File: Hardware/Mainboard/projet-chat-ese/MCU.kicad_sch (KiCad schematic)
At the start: 23 parts, among them J401 Conn_ST_STDC14, J402 USB_C_Receptacle_USB2.0_16P, J403 UART, SW401 SW_SPST, U401 STM32G431CBUx, U402 USBLC6-2SC6, Y401 MCSJK-7U-16.00-10-30-80-B-30

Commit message: On a pas de wiork trtee anyway
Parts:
- J403: footprint Connector_JST:JST_EH_B4B-EH-A_1x04_P2.50mm_Vertical -> Connector_JST:JST_PH_B4B-PH-K_1x04_P2.00mm_Vertical
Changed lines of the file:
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@@
 			)
 		)
-		(property "Footprint" "Connector_JST:JST_EH_B4B-EH-A_1x04_P2.50mm_Vertical"
+		(property "Footprint" "Connector_JST:JST_PH_B4B-PH-K_1x04_P2.00mm_Vertical"
 			(at 213.36 99.06 0)
 			(effects

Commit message: Finishing PCB
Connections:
- net +3.3V: no longer J403.1 (Pin_1)
- net +5V: now also J403.1 (Pin_1)
- net BT_~{RST}: now also U401.39 (PC10); no longer U401.25 (PB12)
- net GND: now also J403.3 (Pin_3)
- net MOT1_Imes: now also U401.11 (PA3); no longer U401.28 (PB15)
- net UART1_Rx: now also J403.2 (Pin_2), U401.38 (PA15); no longer J403.3 (Pin_3), U401.11 (PA3)
- net UART1_Tx: no longer names the net of U401.10 (PA2)
- net UART1_Tx: no longer J403.2 (Pin_2)
- no-connect marks 15 -> 16
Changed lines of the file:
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@@
 	)
 	(junction
+		(at 207.01 104.14)
+		(diameter 0)
+		(color 0 0 0 0)
+	)
+	(junction
 		(at 252.73 151.13)
 		(diameter 0)
@@
 	)
 	(no_connect
-		(at 107.95 82.55)
-	)
-	(no_connect
 		(at 266.7 137.16)
 	)
@@
 	)
 	(no_connect
-		(at 72.39 67.31)
+		(at 72.39 113.03)
 	)
 	(no_connect
@@
 	)
 	(no_connect
+		(at 107.95 49.53)
+	)
+	(no_connect
+		(at 72.39 120.65)
+	)
+	(no_connect
 		(at 72.39 92.71)
 	)
@@
 	(wire
 		(pts
+			(xy 69.85 67.31) (xy 72.39 67.31)
+		)
+		(stroke
+			(width 0)
+			(type default)
+		)
+	)
+	(wire
+		(pts
 			(xy 41.91 52.07) (xy 38.1 52.07)
 		)
@@
 	(wire
 		(pts
-			(xy 69.85 120.65) (xy 72.39 120.65)
+			(xy 207.01 41.91) (xy 214.63 41.91)
 		)
 		(stroke
@@
 	(wire
 		(pts
-			(xy 207.01 41.91) (xy 214.63 41.91)
+			(xy 196.85 99.06) (xy 208.28 99.06)
 		)
 		(stroke
@@
 	(wire
 		(pts
-			(xy 252.73 151.13) (xy 251.46 151.13)
+			(xy 207.01 101.6) (xy 207.01 104.14)
 		)
 		(stroke
@@
 	(wire
 		(pts
-			(xy 72.39 54.61) (xy 66.04 54.61)
+			(xy 252.73 151.13) (xy 251.46 151.13)
 		)
 		(stroke
@@
 	(wire
 		(pts
-			(xy 107.95 57.15) (xy 111.76 57.15)
+			(xy 72.39 54.61) (xy 66.04 54.61)
 		)
 		(stroke
@@
 	(wire
 		(pts
-			(xy 41.91 102.87) (xy 46.99 102.87)
+			(xy 107.95 57.15) (xy 111.76 57.15)
 		)
 		(stroke
@@
 	(wire
 		(pts
-			(xy 208.28 96.52) (xy 207.01 96.52)
+			(xy 41.91 102.87) (xy 46.99 102.87)
 		)
 		(stroke
@@
 	(wire
 		(pts
-			(xy 69.85 107.95) (xy 72.39 107.95)
+			(xy 208.28 96.52) (xy 207.01 96.52)
 		)
 		(stroke
@@
 	(wire
 		(pts
-			(xy 119.38 52.07) (xy 107.95 52.07)
+			(xy 69.85 107.95) (xy 72.39 107.95)
 		)
 		(stroke
@@
 		)
 	)
+	(wire
+		(pts
+			(xy 208.28 101.6) (xy 207.01 101.6)
+		)
+		(stroke
+			(width 0)
+			(type default)
+		)
+	)
 	(polyline
 		(pts
@@
 	(wire
 		(pts
-			(xy 119.38 49.53) (xy 107.95 49.53)
-		)
-		(stroke
-			(width 0)
-			(type default)
-		)
-	)
-	(wire
-		(pts
 			(xy 240.03 38.1) (xy 240.03 40.64)
 		)
@@
 	(wire
 		(pts
-			(xy 69.85 87.63) (xy 72.39 87.63)
+			(xy 111.76 52.07) (xy 107.95 52.07)
 		)
 		(stroke
@@
 	(wire
 		(pts
-			(xy 27.94 106.68) (xy 27.94 102.87)
+			(xy 69.85 87.63) (xy 72.39 87.63)
 		)
 		(stroke
@@
 	(wire
 		(pts
-			(xy 228.6 30.48) (xy 241.3 30.48)
+			(xy 27.94 106.68) (xy 27.94 102.87)
 		)
 		(stroke
@@
 	(wire
 		(pts
-			(xy 219.71 25.4) (xy 219.71 34.29)
+			(xy 228.6 30.48) (xy 241.3 30.48)
 		)
 		(stroke
@@
 	(wire
 		(pts
-			(xy 69.85 105.41) (xy 72.39 105.41)
+			(xy 219.71 25.4) (xy 219.71 34.29)
 		)
 		(stroke
@@
 	(wire
 		(pts
-			(xy 74.93 25.4) (xy 74.93 22.86)
+			(xy 119.38 82.55) (xy 107.95 82.55)
 		)
 		(stroke
@@
 	(wire
 		(pts
-			(xy 107.95 67.31) (xy 111.76 67.31)
+			(xy 69.85 105.41) (xy 72.39 105.41)
 		)
 		(stroke
@@
 	(wire
 		(pts
-			(xy 40.64 102.87) (xy 41.91 102.87)
+			(xy 74.93 25.4) (xy 74.93 22.86)
 		)
 		(stroke
@@
 	(wire
 		(pts
-			(xy 38.1 52.07) (xy 38.1 54.61)
+			(xy 107.95 67.31) (xy 111.76 67.31)
 		)
 		(stroke
@@
 	(wire
 		(pts
-			(xy 252.73 153.67) (xy 252.73 151.13)
+			(xy 40.64 102.87) (xy 41.91 102.87)
 		)
 		(stroke
@@
 	(wire
 		(pts
-			(xy 240.03 38.1) (xy 241.3 38.1)
+			(xy 38.1 52.07) (xy 38.1 54.61)
 		)
 		(stroke
@@
 	(wire
 		(pts
-			(xy 52.07 52.07) (xy 41.91 52.07)
+			(xy 252.73 153.67) (xy 252.73 151.13)
 		)
 		(stroke
@@
 	(wire
 		(pts
-			(xy 196.85 101.6) (xy 208.28 101.6)
+			(xy 240.03 38.1) (xy 241.3 38.1)
 		)
 		(stroke
@@
 	(wire
 		(pts
-			(xy 234.95 57.15) (xy 234.95 68.58)
+			(xy 52.07 52.07) (xy 41.91 52.07)
 		)
 		(stroke
@@
 	(wire
 		(pts
-			(xy 213.36 25.4) (xy 213.36 26.67)
+			(xy 234.95 57.15) (xy 234.95 68.58)
 		)
 		(stroke
@@
 	(wire
 		(pts
-			(xy 196.85 99.06) (xy 208.28 99.06)
+			(xy 213.36 25.4) (xy 213.36 26.67)
 		)
 		(stroke
@@
 	(wire
 		(pts
-			(xy 69.85 113.03) (xy 72.39 113.03)
-		)
-		(stroke
-			(width 0)
-			(type default)
-		)
-	)
-	(wire
-		(pts
 			(xy 107.95 46.99) (xy 111.76 46.99)
 		)
@@
 		)
 	)
-	(label "UART1_Tx"
-		(at 119.38 49.53 180)
-		(effects
-			(font
-				(size 1.27 1.27)
-			)
-			(justify right bottom)
-		)
-	)
 	(label "USB_DP"
 		(at 119.38 74.93 180)
@@
 		)
 	)
-	(label "UART1_Tx"
-		(at 196.85 99.06 0)
-		(effects
-			(font
-				(size 1.27 1.27)
-			)
-			(justify left bottom)
-		)
-	)
 	(label "SWO"
 		(at 274.32 129.54 180)
@@
 		)
 	)
-	(label "UART1_Rx"
-		(at 196.85 101.6 0)
+	(label "SWO"
+		(at 59.69 90.17 0)
 		(effects
 			(font
@@
 		)
 	)
-	(label "SWO"
-		(at 59.69 90.17 0)
+	(label "USB_DN"
+		(at 119.38 72.39 180)
 		(effects
 			(font
 				(size 1.27 1.27)
 			)
-			(justify left bottom)
+			(justify right bottom)
 		)
 	)
 	(label "UART1_Rx"
-		(at 119.38 52.07 180)
+		(at 119.38 82.55 180)
 		(effects
 			(font
@@
 	)
 	(label "USB_DN"
-		(at 119.38 72.39 180)
+		(at 207.01 41.91 0)
 		(effects
 			(font
 				(size 1.27 1.27)
 			)
-			(justify right bottom)
+			(justify left bottom)
 		)
 	)
-	(label "USB_DN"
-		(at 207.01 41.91 0)
+	(label "UART1_Rx"
+		(at 196.85 99.06 0)
 		(effects
 			(font
@@
 	(hierarchical_label "BT_~{RST}"
 		(shape input)
-		(at 69.85 113.03 180)
+		(at 69.85 67.31 180)
 		(effects
 			(font
@@
 	(hierarchical_label "MOT1_Imes"
 		(shape input)
-		(at 69.85 120.65 180)
+		(at 111.76 52.07 0)
 		(effects
 			(font
 				(size 1.27 1.27)
 			)
-			(justify right)
+			(justify left)
 		)
 	)
@@
 			)
 		)
-		(property "Value" "+3.3V"
+		(property "Value" "+5V"
 			(at 207.01 90.17 0)
 			(effects

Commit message: check pcb kenny LF
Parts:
- removed C401: 10n, Capacitor_SMD:C_0402_1005Metric, symbol Device:C_Small
- removed R401: 100k, Resistor_SMD:R_0402_1005Metric, symbol Device:R_Small
- removed SW401: SW_SPST, Button_Switch_SMD:SW_Push_1P1T_NO_CK_KSC6xxJ, symbol Switch:SW_SPST
- added L1: 39n, Inductor_SMD:L_0603_1608Metric, symbol Device:L_Small
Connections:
- net +3.3V: now also L1.1; no longer C415.2, C416.2, U401.21 (VDDA)
- net GND: now also C416.2; no longer C416.1
- net BLE_CONFIG: now reaches U401.32 (PA10)
- new net STM32_VDDA: C415.2, C416.1, L1.2, U401.21 (VDDA)
- no-connect marks 16 -> 15
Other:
- moved on the sheet: C410, C411, C412, C413, C414, C415, C416

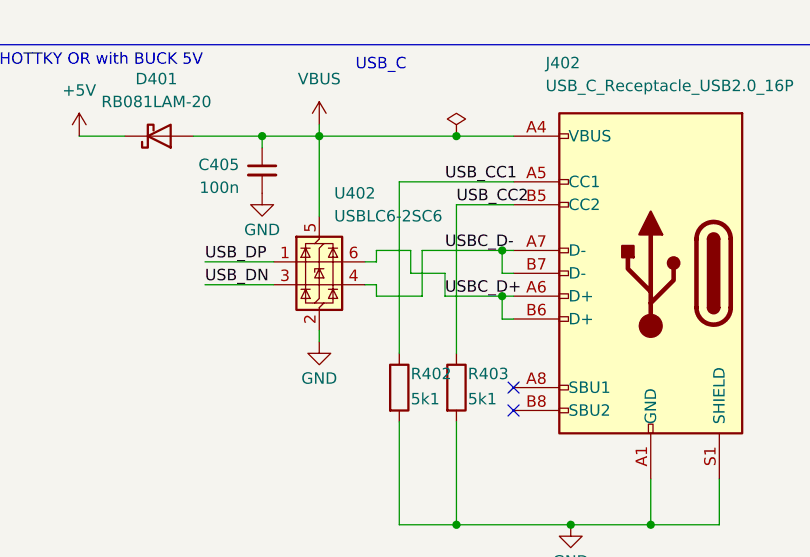
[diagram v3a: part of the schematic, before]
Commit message: Last PCB edits G431
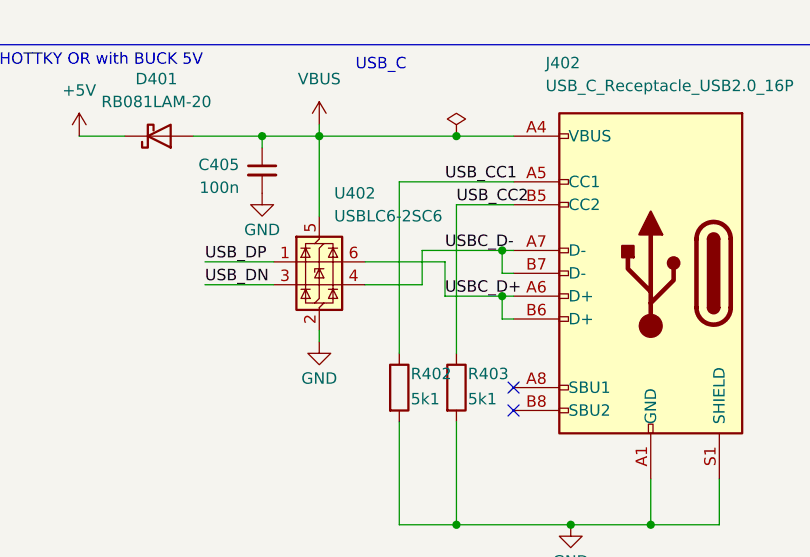
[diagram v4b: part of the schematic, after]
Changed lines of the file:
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@@
 	(wire
 		(pts
-			(xy 224.79 41.91) (xy 226.06 41.91)
+			(xy 224.79 41.91) (xy 231.14 41.91)
 		)
 		(stroke
@@
 	(wire
 		(pts
-			(xy 224.79 39.37) (xy 226.06 39.37)
+			(xy 224.79 39.37) (xy 233.68 39.37)
 		)
 		(stroke
@@
 	(wire
 		(pts
-			(xy 226.06 43.18) (xy 231.14 43.18)
-		)
-		(stroke
-			(width 0)
-			(type default)
-		)
-	)
-	(wire
-		(pts
 			(xy 38.1 64.77) (xy 43.18 64.77)
 		)
@@
 	(wire
 		(pts
-			(xy 233.68 40.64) (xy 233.68 43.18)
+			(xy 233.68 39.37) (xy 233.68 43.18)
 		)
 		(stroke
@@
 	(wire
 		(pts
-			(xy 231.14 43.18) (xy 231.14 38.1)
+			(xy 231.14 41.91) (xy 231.14 38.1)
 		)
 		(stroke
@@
 	(wire
 		(pts
-			(xy 226.06 39.37) (xy 226.06 38.1)
-		)
-		(stroke
-			(width 0)
-			(type default)
-		)
-	)
-	(wire
-		(pts
 			(xy 76.2 22.86) (xy 85.09 22.86)
 		)
@@
 	(wire
 		(pts
-			(xy 226.06 38.1) (xy 229.87 38.1)
-		)
-		(stroke
-			(width 0)
-			(type default)
-		)
-	)
-	(wire
-		(pts
 			(xy 95.25 26.67) (xy 95.25 29.21)
 		)
@@
 	(wire
 		(pts
-			(xy 229.87 40.64) (xy 233.68 40.64)
-		)
-		(stroke
-			(width 0)
-			(type default)
-		)
-	)
-	(wire
-		(pts
 			(xy 67.31 59.69) (xy 67.31 57.15)
 		)
@@
 	(wire
 		(pts
-			(xy 226.06 41.91) (xy 226.06 43.18)
-		)
-		(stroke
-			(width 0)
-			(type default)
-		)
-	)
-	(wire
-		(pts
 			(xy 48.26 22.86) (xy 48.26 25.4)
 		)
@@
 		)
 		(stroke
-			(width 0)
-			(type default)
-		)
-	)
-	(wire
-		(pts
-			(xy 229.87 38.1) (xy 229.87 40.64)
-		)
-		(stroke

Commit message: G431
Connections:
- net GND: no longer J403.3 (Pin_3)
- net Lidar_speed: now reaches U401.44 (PB6)
- net Lidar_speed: now also J403.3 (Pin_3)
- no-connect marks 15 -> 14
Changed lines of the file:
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@@
-	)
-	(junction
-		(at 207.01 104.14)
-		(diameter 0)
-		(color 0 0 0 0)
 	)
 	(junction
@@
 	)
 	(no_connect
-		(at 72.39 97.79)
-	)
-	(no_connect
 		(at 266.7 144.78)
 	)
@@
 	(wire
 		(pts
-			(xy 196.85 99.06) (xy 208.28 99.06)
+			(xy 194.31 99.06) (xy 208.28 99.06)
 		)
 		(stroke
@@
 	(wire
 		(pts
-			(xy 207.01 101.6) (xy 207.01 104.14)
-		)
-		(stroke
-			(width 0)
-			(type default)
-		)
-	)
-	(wire
-		(pts
 			(xy 252.73 151.13) (xy 251.46 151.13)
 		)
@@
 	(wire
 		(pts
+			(xy 59.69 97.79) (xy 72.39 97.79)
+		)
+		(stroke
+			(width 0)
+			(type default)
+		)
+	)
+	(wire
+		(pts
 			(xy 69.85 102.87) (xy 72.39 102.87)
 		)
@@
 		)
 	)
-	(wire
-		(pts
-			(xy 208.28 101.6) (xy 207.01 101.6)
-		)
-		(stroke
-			(width 0)
-			(type default)
-		)
-	)
 	(polyline
 		(pts
@@
 		(pts
 			(xy 110.49 26.67) (xy 100.33 26.67)
+		)
+		(stroke
+			(width 0)
+			(type default)
+		)
+	)
+	(wire
+		(pts
+			(xy 194.31 101.6) (xy 208.28 101.6)
 		)
 		(stroke
@@
 		)
 	)
+	(label "Lidar_speed"
+		(at 194.31 101.6 0)
+		(effects
+			(font
+				(size 1.27 1.27)
+			)
+			(justify left bottom)
+		)
+	)
 	(label "NRST"
 		(at 55.88 49.53 0)
@@
 		)
 	)
+	(label "Lidar_speed"
+		(at 59.69 97.79 0)
+		(effects
+			(font
+				(size 1.27 1.27)
+			)
+			(justify left bottom)
+		)
+	)
 	(label "USB_DN"
 		(at 119.38 72.39 180)
@@
 	)
 	(label "UART1_Rx"
-		(at 196.85 99.06 0)
+		(at 194.31 99.06 0)
 		(effects
 			(font

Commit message: Kenny's Last work
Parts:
- added D104: GR, LED_SMD:LED_0603_1608Metric, symbol Device:LED
- added R108: 1k, Resistor_SMD:R_0402_1005Metric, symbol Device:R
- added R109: 100k, Resistor_SMD:R_0402_1005Metric, symbol Device:R
- added SW401: SW_Push_SPDT, symbol Switch:SW_Push_SPDT
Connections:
- net +3.3V: now also D104.1 (K)
- net GND: now also R109.2
- net ToF_SCL: now also SW401.3 (C); no longer U401.46 (PB8)
- net user_led: now reaches U401.3 (PC14)
- net user_led: now also R108.1
- new net: R109.1, SW401.1 (A)
- new net: D104.2 (A), R108.2
- new net PB8: SW401.2 (B), U401.46 (PB8)
- no-connect marks 14 -> 13
